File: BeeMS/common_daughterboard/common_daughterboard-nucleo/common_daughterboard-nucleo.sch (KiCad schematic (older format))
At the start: 28 parts, among them J1 OUT_CONN, J2 TERM, J3 IN_CONN, J4 HEAD, J5 TAIL, J6 Conn_02x10_Odd_Even, Q1 BSS138, Q2 BSS138, U1 MCP2558FD-xSN

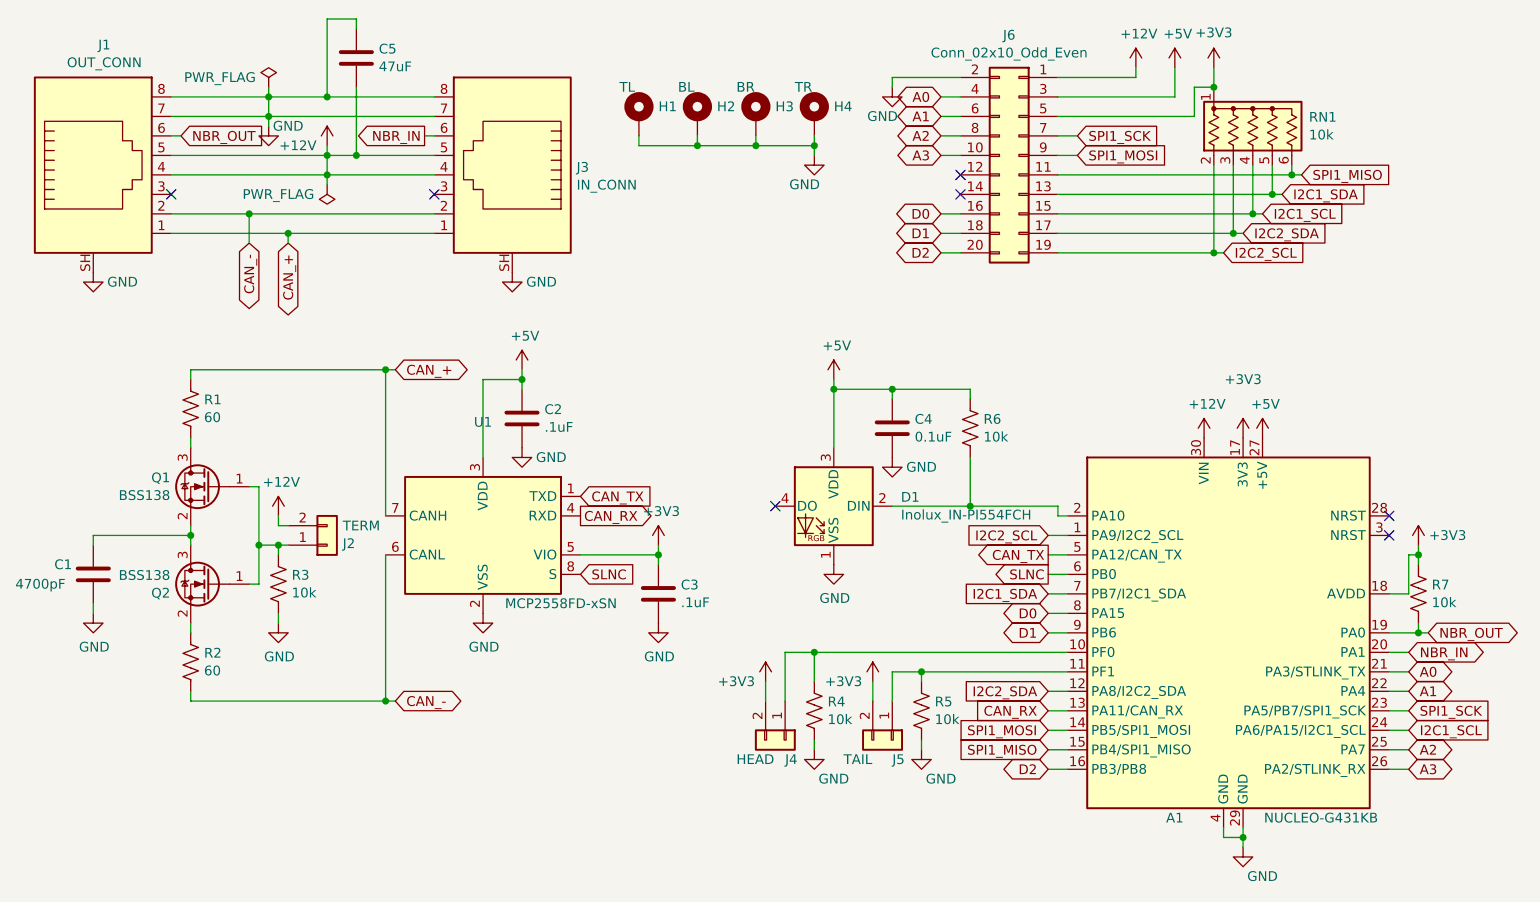
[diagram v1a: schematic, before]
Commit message: Added BOM for the nucleo common daughterboard
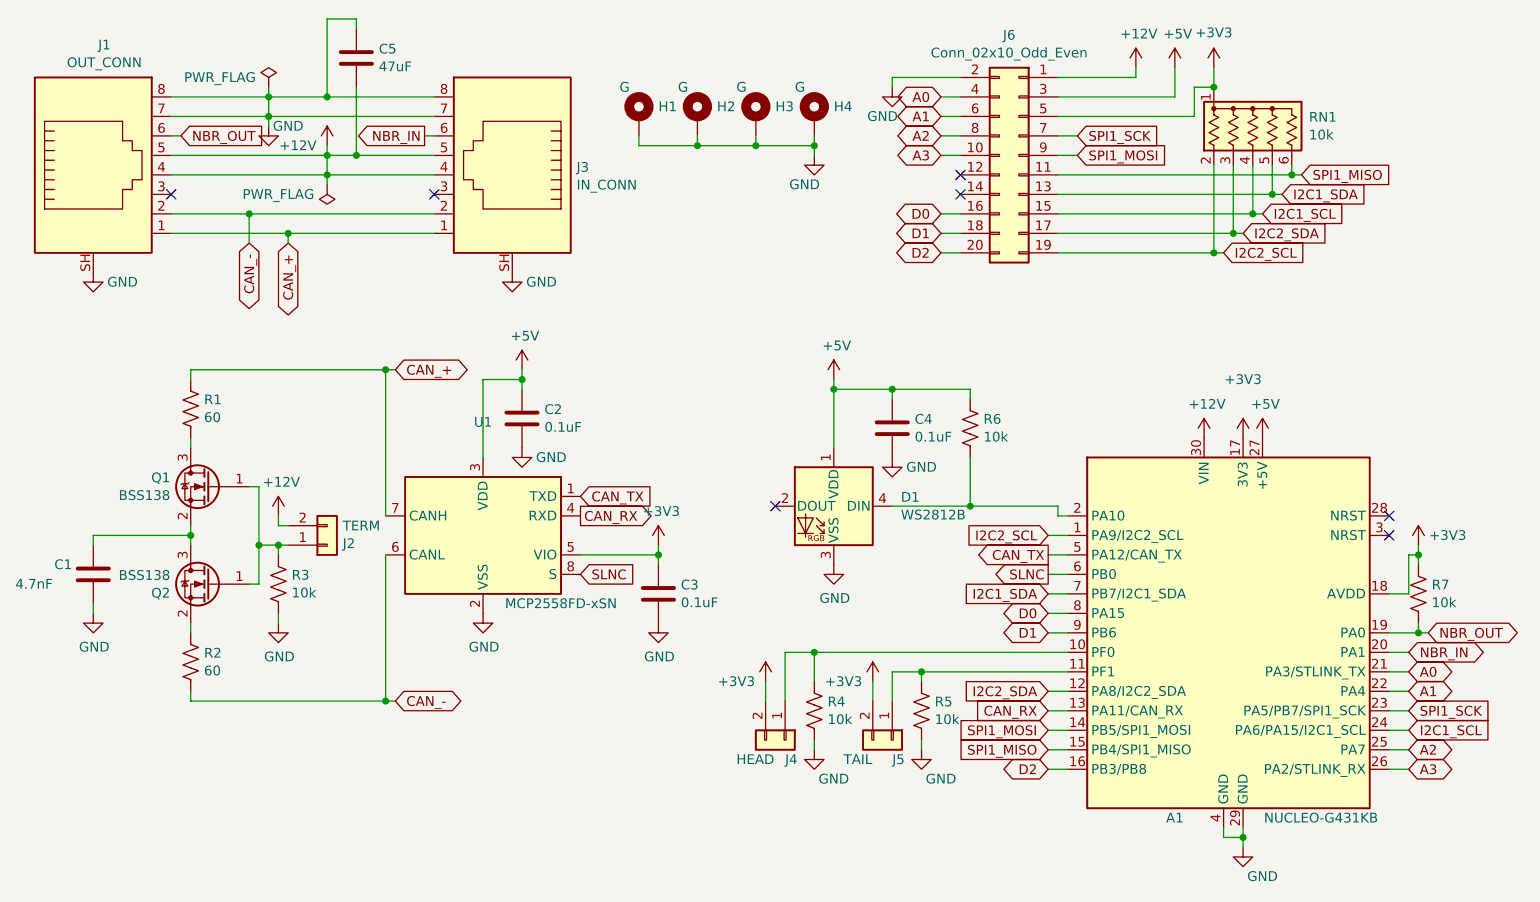
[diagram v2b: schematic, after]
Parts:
- removed D1: Inolux_IN-PI554FCH, LED_SMD:LED_Inolux_IN-PI554FCH_PLCC4_5.0x5.0mm_P3.2mm, symbol LED:Inolux_IN-PI554FCH
- added D1: WS2812B, LED_SMD:LED_WS2812B_PLCC4_5.0x5.0mm_P3.2mm, symbol LED:WS2812B
- A1: Digi-Key_PN (none) -> 497-19489-ND; MPN (none) -> NUCLEO-G431KB
- C1: value 4700pF -> 4.7nF; Digi-Key_PN (none) -> 732-8119-1-ND; MPN (none) -> 885012208079
- C2, C3: value .1uF -> 0.1uF; Digi-Key_PN (none) -> 732-8127-1-ND; MPN (none) -> 885012208087
- C4: Digi-Key_PN (none) -> 732-8127-1-ND; MPN (none) -> 885012208087
- C5: Digi-Key_PN (none) -> 490-10531-1-ND; MPN (none) -> RM32EC81C476KE15L
- H1: value TL -> G; fit_field (none) -> DNF
- H2: value BL -> G; fit_field (none) -> DNF
- H3: value BR -> G; fit_field (none) -> DNF
- H4: value TR -> G; fit_field (none) -> DNF
- J1, J3: Digi-Key_PN (none) -> RJHSE-5380-ND; MPN (none) -> RJHSE-5380
- J2, J4, J5: fit_field (none) -> DNF
- J6: Digi-Key_PN (none) -> S9197-ND; MPN (none) -> SFH11-PBPC-D10-ST-BK
- Q1, Q2: Digi-Key_PN (none) -> BSS138CT-ND; MPN (none) -> BSS138CT
- R1, R2: footprint Resistor_SMD:R_1206_3216Metric -> Resistor_SMD:R_1206_3216Metric_Pad1.42x1.75mm_HandSolder; Digi-Key_PN (none) -> P75ALCT-ND; MPN (none) -> ERJ-P08J750V
- R3, R4, R5, R6, R7: Digi-Key_PN (none) -> 311-10KERCT-ND; MPN (none) -> RC1206JR-0710KL
- RN1: Digi-Key_PN (none) -> 4606X-AP1-103LFTB-ND; MPN (none) -> 4606X-AP1-103LF
- U1: Digi-Key_PN (none) -> MCP2558FD-H/SN; MPN (none) -> MCP2558FD-H/SN-ND
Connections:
- net +5V: now also D1.1 (VDD)
- net GND: now also D1.3 (VSS)
- net at A1.2 (PA10), R6.2: now also D1.4 (DIN)
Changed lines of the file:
@@
 F 2 "BeeMS:NUCLEO-G431KB" H 6800 3750 50  0001 C CIN
 F 3 "https://www.st.com/content/ccc/resource/technical/document/user_manual/group1/f7/3c/7f/d1/2a/1c/4f/65/DM00493601/files/DM00493601.pdf/jcr:content/translations/en.DM00493601.pdf" H 6800 3750 50  0001 C CNN
+F 4 "NUCLEO-G431KB" H 6800 3750 50  0001 C CNN "MPN"
+F 5 "497-19489-ND" H 6800 3750 50  0001 C CNN "Digi-Key_PN"
 	1    6800 3750
 	1    0    0    -1
@@
 F 0 "R1" H 1518 2646 50  0000 L CNN
 F 1 "60" H 1518 2555 50  0000 L CNN
-F 2 "Resistor_SMD:R_1206_3216Metric" V 1490 2590 50  0001 C CNN
+F 2 "Resistor_SMD:R_1206_3216Metric_Pad1.42x1.75mm_HandSolder" V 1490 2590 50  0001 C CNN
 F 3 "~" H 1450 2600 50  0001 C CNN
+F 4 "P75ALCT-ND" H 1450 2600 50  0001 C CNN "Digi-Key_PN"
+F 5 "ERJ-P08J750V" H 1450 2600 50  0001 C CNN "MPN"
 	1    1450 2600
 	1    0    0    -1
@@
 F 0 "R2" H 1518 3946 50  0000 L CNN
 F 1 "60" H 1518 3855 50  0000 L CNN
-F 2 "Resistor_SMD:R_1206_3216Metric" V 1490 3890 50  0001 C CNN
+F 2 "Resistor_SMD:R_1206_3216Metric_Pad1.42x1.75mm_HandSolder" V 1490 3890 50  0001 C CNN
 F 3 "~" H 1450 3900 50  0001 C CNN
+F 4 "P75ALCT-ND" H 1450 3900 50  0001 C CNN "Digi-Key_PN"
+F 5 "ERJ-P08J750V" H 1450 3900 50  0001 C CNN "MPN"
 	1    1450 3900
 	1    0    0    -1
@@
 P 950 3450
 F 0 "C1" H 750 3500 50  0000 L CNN
-F 1 "4700pF" H 550 3400 50  0000 L CNN
+F 1 "4.7nF" H 550 3400 50  0000 L CNN
 F 2 "Capacitor_SMD:C_1206_3216Metric_Pad1.42x1.75mm_HandSolder" H 988 3300 50  0001 C CNN
 F 3 "~" H 950 3450 50  0001 C CNN
+F 4 "732-8119-1-ND" H 950 3450 50  0001 C CNN "Digi-Key_PN"
+F 5 "885012208079" H 950 3450 50  0001 C CNN "MPN"
 	1    950  3450
 	1    0    0    -1
@@
 F 2 "Package_TO_SOT_SMD:SOT-23" H 1750 3425 50  0001 L CIN
 F 3 "https://www.fairchildsemi.com/datasheets/BS/BSS138.pdf" H 1550 3500 50  0001 L CNN
+F 4 "BSS138CT-ND" H 1550 3500 50  0001 C CNN "Digi-Key_PN"
+F 5 "BSS138CT" H 1550 3500 50  0001 C CNN "MPN"
 	1    1550 3500
 	-1   0    0    -1
@@
 F 2 "Package_TO_SOT_SMD:SOT-23" H 1750 2925 50  0001 L CIN
 F 3 "https://www.fairchildsemi.com/datasheets/BS/BSS138.pdf" H 1550 3000 50  0001 L CNN
+F 4 "BSS138CT-ND" H 1550 3000 50  0001 C CNN "Digi-Key_PN"
+F 5 "BSS138CT" H 1550 3000 50  0001 C CNN "MPN"
 	1    1550 3000
 	-1   0    0    -1
@@
 F 2 "Connector_PinHeader_2.54mm:PinHeader_1x02_P2.54mm_Vertical" H 2150 3300 50  0001 C CNN
 F 3 "~" H 2150 3300 50  0001 C CNN
+F 4 "" H 2150 3300 50  0001 C CNN "Digi-Key_PN"
+F 5 "" H 2150 3300 50  0001 C CNN "MPN"
+F 6 "DNF" H 2150 3300 50  0001 C CNN "fit_field"
 	1    2150 3300
 	1    0    0    1
@@
 F 2 "Resistor_SMD:R_1206_3216Metric" V 1940 3490 50  0001 C CNN
 F 3 "~" H 1900 3500 50  0001 C CNN
+F 4 "311-10KERCT-ND" H 1900 3500 50  0001 C CNN "Digi-Key_PN"
+F 5 "RC1206JR-0710KL" H 1900 3500 50  0001 C CNN "MPN"
 	1    1900 3500
 	1    0    0    -1
@@
 P 3850 3550
 F 0 "C3" H 3965 3596 50  0000 L CNN
-F 1 ".1uF" H 3965 3505 50  0000 L CNN
+F 1 "0.1uF" H 3965 3505 50  0000 L CNN
 F 2 "Capacitor_SMD:C_1206_3216Metric_Pad1.42x1.75mm_HandSolder" H 3888 3400 50  0001 C CNN
 F 3 "~" H 3850 3550 50  0001 C CNN
+F 4 "732-8127-1-ND" H 3850 3550 50  0001 C CNN "Digi-Key_PN"
+F 5 "885012208087" H 3850 3550 50  0001 C CNN "MPN"
 	1    3850 3550
 	1    0    0    -1
@@
 $EndComp
 $Comp
-L LED:Inolux_IN-PI554FCH D1
-U 1 1 5E471372
-P 4750 3100
-F 0 "D1" H 4406 3146 50  0000 R CNN
-F 1 "Inolux_IN-PI554FCH" H 4406 3055 50  0000 R CNN
-F 2 "LED_SMD:LED_Inolux_IN-PI554FCH_PLCC4_5.0x5.0mm_P3.2mm" H 4800 2800 50  0001 L TNN
-F 3 "http://www.inolux-corp.com/datasheet/SMDLED/Addressable%20LED/IN-PI554FCH.pdf" H 4850 2725 50  0001 L TNN
-	1    4750 3100
-	-1   0    0    -1
-$EndComp
-$Comp
 L power:GND #PWR016
 U 1 1 5E493AD9
@@
 F 2 "Capacitor_SMD:C_1206_3216Metric_Pad1.42x1.75mm_HandSolder" H 5088 2550 50  0001 C CNN
 F 3 "~" H 5050 2700 50  0001 C CNN
+F 4 "732-8127-1-ND" H 5050 2700 50  0001 C CNN "Digi-Key_PN"
+F 5 "885012208087" H 5050 2700 50  0001 C CNN "MPN"
 	1    5050 2700
 	1    0    0    -1
@@
 F 2 "Resistor_SMD:R_1206_3216Metric" V 5490 2690 50  0001 C CNN
 F 3 "~" H 5450 2700 50  0001 C CNN
+F 4 "311-10KERCT-ND" H 5450 2700 50  0001 C CNN "Digi-Key_PN"
+F 5 "RC1206JR-0710KL" H 5450 2700 50  0001 C CNN "MPN"
 	1    5450 2700
 	1    0    0    -1
@@
 F 2 "Connector_PinHeader_2.54mm:PinHeader_1x02_P2.54mm_Vertical" H 5050 4300 50  0001 C CNN
 F 3 "~" H 5050 4300 50  0001 C CNN
+F 4 "" H 5050 4300 50  0001 C CNN "Digi-Key_PN"
+F 5 "" H 5050 4300 50  0001 C CNN "MPN"
+F 6 "DNF" H 5050 4300 50  0001 C CNN "fit_field"
 	1    5050 4300
 	0    1    1    0
@@
 F 2 "Connector_PinHeader_2.54mm:PinHeader_1x02_P2.54mm_Vertical" H 4500 4300 50  0001 C CNN
 F 3 "~" H 4500 4300 50  0001 C CNN
+F 4 "" H 4500 4300 50  0001 C CNN "Digi-Key_PN"
+F 5 "" H 4500 4300 50  0001 C CNN "MPN"
+F 6 "DNF" H 4500 4300 50  0001 C CNN "fit_field"
 	1    4500 4300
 	0    1    1    0
@@
 F 2 "Resistor_SMD:R_1206_3216Metric" V 5240 4140 50  0001 C CNN
 F 3 "~" H 5200 4150 50  0001 C CNN
+F 4 "311-10KERCT-ND" H 5200 4150 50  0001 C CNN "Digi-Key_PN"
+F 5 "RC1206JR-0710KL" H 5200 4150 50  0001 C CNN "MPN"
 	1    5200 4150
 	1    0    0    -1
@@
 F 2 "Resistor_SMD:R_1206_3216Metric" V 4690 4140 50  0001 C CNN
 F 3 "~" H 4650 4150 50  0001 C CNN
+F 4 "311-10KERCT-ND" H 4650 4150 50  0001 C CNN "Digi-Key_PN"
+F 5 "RC1206JR-0710KL" H 4650 4150 50  0001 C CNN "MPN"
 	1    4650 4150
 	1    0    0    -1
@@
 F 2 "Package_SO:SOIC-8_3.9x4.9mm_P1.27mm" H 2950 2650 50  0001 C CNN
 F 3 "https://ww1.microchip.com/downloads/en/DeviceDoc/20005533A.pdf" H 2950 3250 50  0001 C CNN
+F 4 "MCP2558FD-H/SN" H 2950 3250 50  0001 C CNN "Digi-Key_PN"
+F 5 "MCP2558FD-H/SN-ND" H 2950 3250 50  0001 C CNN "MPN"
 	1    2950 3250
 	-1   0    0    -1
@@
 P 3150 2650
 F 0 "C2" H 3265 2696 50  0000 L CNN
-F 1 ".1uF" H 3265 2605 50  0000 L CNN
+F 1 "0.1uF" H 3265 2605 50  0000 L CNN
 F 2 "Capacitor_SMD:C_1206_3216Metric_Pad1.42x1.75mm_HandSolder" H 3188 2500 50  0001 C CNN
 F 3 "~" H 3150 2650 50  0001 C CNN
+F 4 "732-8127-1-ND" H 3150 2650 50  0001 C CNN "Digi-Key_PN"
+F 5 "885012208087" H 3150 2650 50  0001 C CNN "MPN"
 	1    3150 2650
 	1    0    0    -1
@@
 F 2 "Resistor_SMD:R_1206_3216Metric" V 7790 3540 50  0001 C CNN
 F 3 "~" H 7750 3550 50  0001 C CNN
+F 4 "311-10KERCT-ND" H 7750 3550 50  0001 C CNN "Digi-Key_PN"
+F 5 "RC1206JR-0710KL" H 7750 3550 50  0001 C CNN "MPN"
 	1    7750 3550
 	1    0    0    -1
@@
 F 2 "Connector_RJ:RJ45_Amphenol_RJHSE5380" V 950 1425 50  0001 C CNN
 F 3 "~" V 950 1425 50  0001 C CNN
+F 4 "RJHSE-5380-ND" H 950 1400 50  0001 C CNN "Digi-Key_PN"
+F 5 "RJHSE-5380" H 950 1400 50  0001 C CNN "MPN"
 	1    950  1400
 	1    0    0    -1
@@
 F 2 "Connector_RJ:RJ45_Amphenol_RJHSE5380" V 3100 1425 50  0001 C CNN
 F 3 "~" V 3100 1425 50  0001 C CNN
+F 4 "RJHSE-5380-ND" H 3100 1400 50  0001 C CNN "Digi-Key_PN"
+F 5 "RJHSE-5380" H 3100 1400 50  0001 C CNN "MPN"
 	1    3100 1400
 	-1   0    0    -1
@@
 P 3750 1100
 F 0 "H1" H 3850 1150 50  0000 L CNN
-F 1 "TL" H 3650 1250 50  0000 L CNN
+F 1 "G" H 3650 1250 50  0000 L CNN
 F 2 "MountingHole:MountingHole_2.2mm_M2_ISO7380_Pad" H 3750 1100 50  0001 C CNN
 F 3 "~" H 3750 1100 50  0001 C CNN
+F 4 "" H 3750 1100 50  0001 C CNN "Digi-Key_PN"
+F 5 "" H 3750 1100 50  0001 C CNN "MPN"
+F 6 "DNF" H 3750 1100 50  0001 C CNN "fit_field"
 	1    3750 1100
 	1    0    0    -1
@@
 P 4050 1100
 F 0 "H2" H 4150 1150 50  0000 L CNN
-F 1 "BL" H 3950 1250 50  0000 L CNN
+F 1 "G" H 3950 1250 50  0000 L CNN
 F 2 "MountingHole:MountingHole_2.2mm_M2_ISO7380_Pad" H 4050 1100 50  0001 C CNN
 F 3 "~" H 4050 1100 50  0001 C CNN
+F 4 "" H 4050 1100 50  0001 C CNN "Digi-Key_PN"
+F 5 "" H 4050 1100 50  0001 C CNN "MPN"
+F 6 "DNF" H 4050 1100 50  0001 C CNN "fit_field"
 	1    4050 1100
 	1    0    0    -1
@@
 P 4350 1100
 F 0 "H3" H 4450 1150 50  0000 L CNN
-F 1 "BR" H 4250 1250 50  0000 L CNN
+F 1 "G" H 4250 1250 50  0000 L CNN
 F 2 "MountingHole:MountingHole_2.2mm_M2_ISO7380_Pad" H 4350 1100 50  0001 C CNN
 F 3 "~" H 4350 1100 50  0001 C CNN
+F 4 "" H 4350 1100 50  0001 C CNN "Digi-Key_PN"
+F 5 "" H 4350 1100 50  0001 C CNN "MPN"
+F 6 "DNF" H 4350 1100 50  0001 C CNN "fit_field"
 	1    4350 1100
 	1    0    0    -1
@@
 P 4650 1100
 F 0 "H4" H 4750 1150 50  0000 L CNN
-F 1 "TR" H 4550 1250 50  0000 L CNN
+F 1 "G" H 4550 1250 50  0000 L CNN
 F 2 "MountingHole:MountingHole_2.2mm_M2_ISO7380_Pad" H 4650 1100 50  0001 C CNN
 F 3 "~" H 4650 1100 50  0001 C CNN
+F 4 "" H 4650 1100 50  0001 C CNN "Digi-Key_PN"
+F 5 "" H 4650 1100 50  0001 C CNN "MPN"
+F 6 "DNF" H 4650 1100 50  0001 C CNN "fit_field"
 	1    4650 1100
 	1    0    0    -1
@@
 F 2 "Resistor_THT:R_Array_SIP6" V 7275 1150 50  0001 C CNN
 F 3 "http://www.vishay.com/docs/31509/csc.pdf" H 6900 1150 50  0001 C CNN
+F 4 "4606X-AP1-103LFTB-ND" H 6900 1150 50  0001 C CNN "Digi-Key_PN"
+F 5 "4606X-AP1-103LF" H 6900 1150 50  0001 C CNN "MPN"
 	1    6900 1150
 	1    0    0    -1
@@
 F 2 "Connector_PinHeader_2.54mm:PinHeader_2x10_P2.54mm_Vertical" H 5700 1300 50  0001 C CNN
 F 3 "~" H 5700 1300 50  0001 C CNN
+F 4 "S9197-ND" H 5700 1300 50  0001 C CNN "Digi-Key_PN"
+F 5 "SFH11-PBPC-D10-ST-BK" H 5700 1300 50  0001 C CNN "MPN"
 	1    5700 1300
 	-1   0    0    -1
@@
 F 2 "Capacitor_SMD:C_1210_3225Metric_Pad1.42x2.65mm_HandSolder" H 2338 650 50  0001 C CNN
 F 3 "~" H 2300 800 50  0001 C CNN
+F 4 "490-10531-1-ND" H 2300 800 50  0001 C CNN "Digi-Key_PN"
+F 5 "RM32EC81C476KE15L" H 2300 800 50  0001 C CNN "MPN"
 	1    2300 800
 	1    0    0    -1
@@
 Wire Wire Line
 	2150 1000 2700 1000
+$Comp
+L LED:WS2812B D1
+U 1 1 5E51E097
+P 4750 3100
+F 0 "D1" H 4406 3146 50  0000 R CNN
+F 1 "WS2812B" H 4406 3055 50  0000 R CNN
+F 2 "LED_SMD:LED_WS2812B_PLCC4_5.0x5.0mm_P3.2mm" H 4800 2800 50  0001 L TNN
+F 3 "https://cdn-shop.adafruit.com/datasheets/WS2812B.pdf" H 4850 2725 50  0001 L TNN
+F 4 "1568-1800-ND" H 4750 3100 50  0001 C CNN "Digi-Key_PN"
+F 5 "COM-11821" H 4750 3100 50  0001 C CNN "MPN"
+	1    4750 3100
+	-1   0    0    -1
+$EndComp
 $EndSCHEMATC
